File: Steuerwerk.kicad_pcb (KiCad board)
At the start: 2 copper layers, 100 x 160 mm, 332 parts, among them J1 Conn_01x04, J2 Conn_01x02, J3 Conn_01x03, J4 Conn_01x03, J5 Conn_01x02, J6 Conn_01x04, J7 Conn_01x02, J8 Conn_01x04, J9 Conn_01x02, Q1 Q_PNP_BCE, U1 74LS161, U2 74LS138, U3 74LS138, U4 74240, U5 74LS374, U6 74LS374, U7 74541, U8 74541

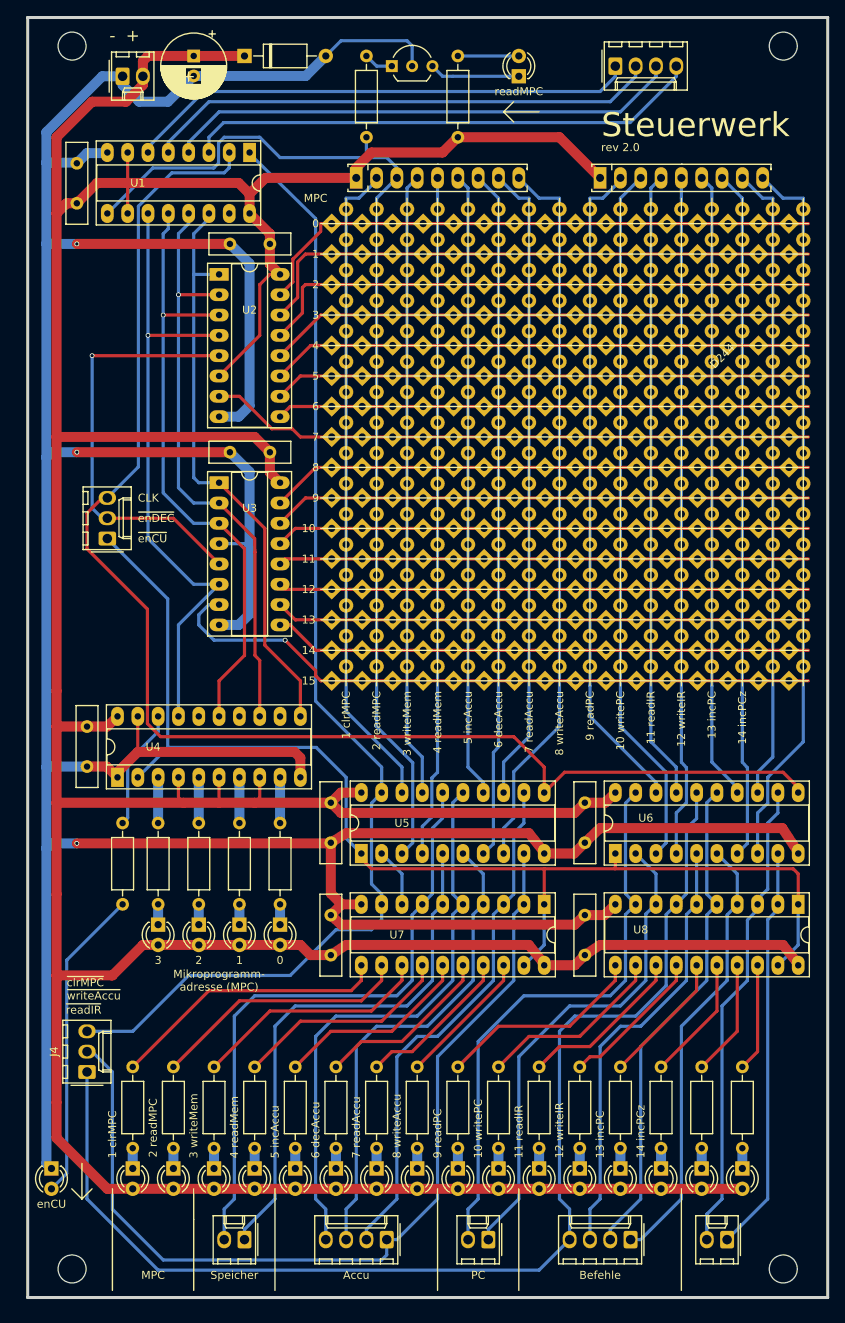
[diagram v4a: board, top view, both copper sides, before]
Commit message: Footprint EuroBoard gedreht und auf das Gitter gelegt (Ursprung links oben)
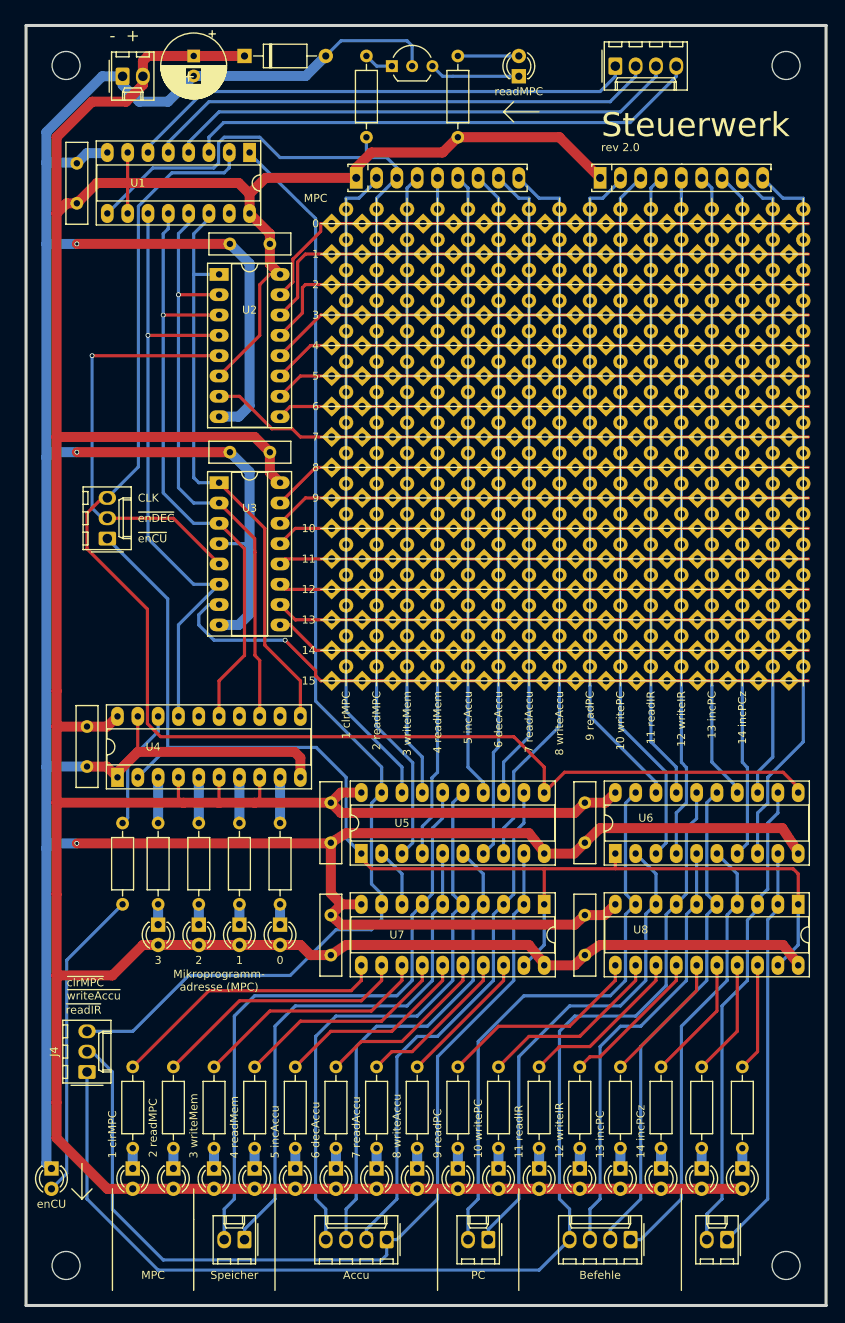
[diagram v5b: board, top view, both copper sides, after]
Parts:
- moved REF** 187.9 mm to (41.3, 33.6), turned to 0 degrees

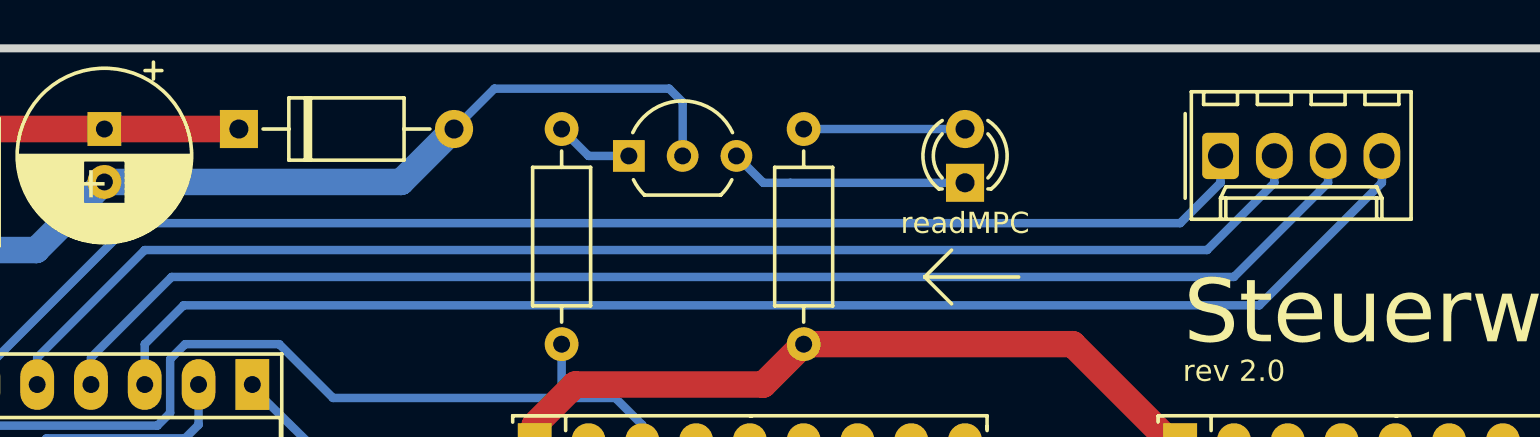
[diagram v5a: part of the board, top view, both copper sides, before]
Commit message: Befehle: An der Platine weitergearbeitet
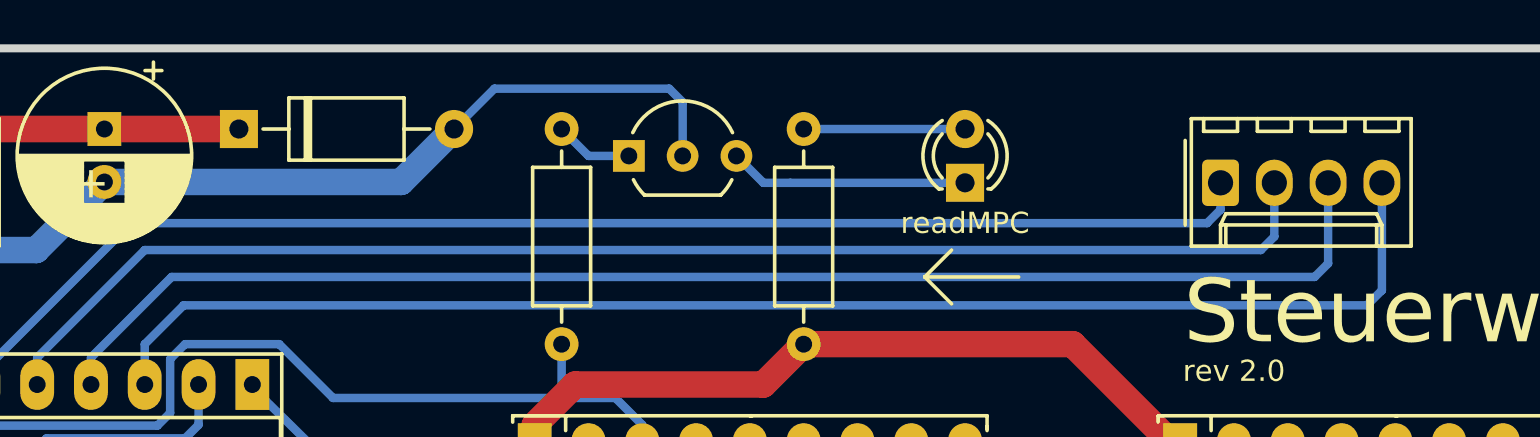
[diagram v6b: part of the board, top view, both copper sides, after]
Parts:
- moved J1 1.27 mm to (115.0, 40.0)
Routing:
- net Net-(J1-Pad4): track 64.8 -> 66.5 mm
- net Net-(J1-Pad3): track 64.4 -> 65.3 mm
- net Net-(J1-Pad1): track 64.0 -> 63.5 mm
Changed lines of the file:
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@@
   )
   (setup
-    (last_trace_width 1.25)
+    (last_trace_width 0.4)
     (user_trace_width 0.2)
     (user_trace_width 0.4)
@@
     (solder_mask_min_width 0.25)
     (aux_axis_origin 0 0)
-    (grid_origin 82.586 52.665998)
+    (grid_origin 41.311 33.615998)
     (visible_elements 7FFFFFFF)
     (pcbplotparams
@@
   )
   (module Connector_Molex:Molex_KK-254_AE-6410-04A_1x04_P2.54mm_Vertical (layer F.Cu)
-    (at 114.971 38.695998)
+    (at 114.971 39.965998)
     (descr "Molex KK-254 Interconnect System, old/engineering part number: AE-6410-04A example for new part number: 22-27-2041, 4 Pins (http://www.molex.com/pdm_docs/sd/022272021_sd.pdf), generated with kicad-footprint-generator")
     (tags "connector Molex KK-254 vertical")
@@
   (segment (start 93.381 39.965998) (end 94.651 39.965998) (width 0.4) (layer B.Cu) (net 21))
   (segment (start 92.111 38.695998) (end 93.381 39.965998) (width 0.4) (layer B.Cu) (net 21))
-  (segment (start 64.171 43.140998) (end 114.336 43.140998) (width 0.4) (layer B.Cu) (net 22))
-  (segment (start 59.091 48.220998) (end 64.171 43.140998) (width 0.4) (layer B.Cu) (net 22))
-  (segment (start 117.511 39.965998) (end 117.511 38.695998) (width 0.4) (layer B.Cu) (net 22))
-  (segment (start 114.336 43.140998) (end 117.511 39.965998) (width 0.4) (layer B.Cu) (net 22))
   (segment (start 59.091 49.490998) (end 59.091 48.220998) (width 0.4) (layer B.Cu) (net 22))
-  (segment (start 113.066 41.870998) (end 114.971 39.965998) (width 0.4) (layer B.Cu) (net 23))
-  (segment (start 63.536 41.870998) (end 113.066 41.870998) (width 0.4) (layer B.Cu) (net 23))
+  (segment (start 59.091 48.220998) (end 64.171 43.140998) (width 0.4) (layer B.Cu) (net 22))
+  (segment (start 64.171 43.140998) (end 116.876 43.140998) (width 0.4) (layer B.Cu) (net 22))
+  (segment (start 117.511 42.505998) (end 117.511 39.965998) (width 0.4) (layer B.Cu) (net 22))
+  (segment (start 116.876 43.140998) (end 117.511 42.505998) (width 0.4) (layer B.Cu) (net 22))
+  (segment (start 114.971 41.235998) (end 114.971 39.965998) (width 0.4) (layer B.Cu) (net 23))
+  (segment (start 114.336 41.870998) (end 114.971 41.235998) (width 0.4) (layer B.Cu) (net 23))
+  (segment (start 63.536 41.870998) (end 114.336 41.870998) (width 0.4) (layer B.Cu) (net 23))
   (segment (start 56.551 48.855998) (end 63.536 41.870998) (width 0.4) (layer B.Cu) (net 23))
-  (segment (start 114.971 39.965998) (end 114.971 38.695998) (width 0.4) (layer B.Cu) (net 23))
   (segment (start 56.551 49.490998) (end 56.551 48.855998) (width 0.4) (layer B.Cu) (net 23))
   (segment (start 126.401 142.200998) (end 127.671 143.470998) (width 0.4) (layer B.Cu) (net 24))
@@
   (segment (start 123.226 180.300998) (end 118.146 185.380998) (width 0.4) (layer B.Cu) (net 25))
   (segment (start 118.146 185.380998) (end 116.876 185.380998) (width 0.4) (layer B.Cu) (net 25))
-  (segment (start 122.591 39.965998) (end 122.591 38.695998) (width 0.4) (layer B.Cu) (net 26))
-  (segment (start 116.806001 45.750997) (end 122.591 39.965998) (width 0.4) (layer B.Cu) (net 26))
-  (segment (start 66.006001 45.750997) (end 116.806001 45.750997) (width 0.4) (layer B.Cu) (net 26))
+  (segment (start 122.591 45.045998) (end 122.591 39.965998) (width 0.4) (layer B.Cu) (net 26))
+  (segment (start 121.886001 45.750997) (end 122.591 45.045998) (width 0.4) (layer B.Cu) (net 26))
+  (segment (start 66.006001 45.750997) (end 121.886001 45.750997) (width 0.4) (layer B.Cu) (net 26))
   (segment (start 64.171 47.585998) (end 66.006001 45.750997) (width 0.4) (layer B.Cu) (net 26))
   (segment (start 64.171 49.490998) (end 64.171 47.585998) (width 0.4) (layer B.Cu) (net 26))
-  (segment (start 120.051 39.965998) (end 120.051 38.695998) (width 0.4) (layer B.Cu) (net 27))
-  (segment (start 115.606 44.410998) (end 120.051 39.965998) (width 0.4) (layer B.Cu) (net 27))
-  (segment (start 65.441 44.410998) (end 115.606 44.410998) (width 0.4) (layer B.Cu) (net 27))
+  (segment (start 120.051 43.775998) (end 120.051 39.965998) (width 0.4) (layer B.Cu) (net 27))
+  (segment (start 119.416 44.410998) (end 120.051 43.775998) (width 0.4) (layer B.Cu) (net 27))
+  (segment (start 65.441 44.410998) (end 119.416 44.410998) (width 0.4) (layer B.Cu) (net 27))
   (segment (start 61.631 48.220998) (end 65.441 44.410998) (width 0.4) (layer B.Cu) (net 27))
   (segment (start 61.631 49.490998) (end 61.631 48.220998) (width 0.4) (layer B.Cu) (net 27))

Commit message: Steuerwerk 2.0 gerber exportiert
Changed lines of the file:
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@@
   )
   (setup
-    (last_trace_width 0.4)
+    (last_trace_width 1.25)
     (user_trace_width 0.2)
     (user_trace_width 0.4)
@@
     (visible_elements 7FFFFFFF)
     (pcbplotparams
-      (layerselection 0x00030_ffffffff)
+      (layerselection 0x010f0_ffffffff)
       (usegerberextensions false)
       (usegerberattributes false)
@@
       (psa4output false)
       (plotreference true)
-      (plotvalue true)
+      (plotvalue false)
       (plotinvisibletext false)
-      (padsonsilk false)
+      (padsonsilk true)
       (subtractmaskfromsilk false)
-      (outputformat 4)
+      (outputformat 1)
       (mirror false)
-      (drillshape 2)
+      (drillshape 0)
       (scaleselection 1)
-      (outputdirectory "C:/Users/Michael/Desktop/gerber-test/"))
+      (outputdirectory "gerber/Steuerwerk 2.0/"))
   )
   (net 0 "")
@@
     (descr "16-lead though-hole mounted DIP package, row spacing 7.62 mm (300 mils), Socket, LongPads")
     (tags "THT DIP DIL PDIP 2.54mm 7.62mm 300mil Socket LongPads")
-    (fp_text reference U3 (at 3.81 3.175) (layer F.SilkS)
+    (fp_text reference U3 (at 3.81 4.445) (layer F.SilkS)
       (effects (font (size 1 1) (thickness 0.17)))
     )
@@
     (descr "20-lead though-hole mounted DIP package, row spacing 7.62 mm (300 mils), Socket, LongPads")
     (tags "THT DIP DIL PDIP 2.54mm 7.62mm 300mil Socket LongPads")
-    (fp_text reference U6 (at 4.445 3.81 180) (layer F.SilkS)
+    (fp_text reference U6 (at 3.81 4.445 180) (layer F.SilkS)
       (effects (font (size 1 1) (thickness 0.17)))
     )
@@
     (descr "20-lead though-hole mounted DIP package, row spacing 7.62 mm (300 mils), Socket, LongPads")
     (tags "THT DIP DIL PDIP 2.54mm 7.62mm 300mil Socket LongPads")
-    (fp_text reference U8 (at 3.175 19.685 180) (layer F.SilkS)
+    (fp_text reference U8 (at 3.81 18.415 180) (layer F.SilkS)
       (effects (font (size 1 1) (thickness 0.17)))
     )
@@
     (effects (font (size 1 1) (thickness 0.17)))
   )
-  (gr_line (start 101.001 44.410998) (end 102.271 45.680998) (layer F.SilkS) (width 0.17))
-  (gr_line (start 102.271 43.140998) (end 101.001 44.410998) (layer F.SilkS) (width 0.17))
-  (gr_line (start 105.446 44.410998) (end 101.001 44.410998) (layer F.SilkS) (width 0.17))
+  (gr_line (start 101.001 44.410998) (end 102.271 45.680998) (layer F.SilkS) (width 0.4))
+  (gr_line (start 102.271 43.140998) (end 101.001 44.410998) (layer F.SilkS) (width 0.4))
+  (gr_line (start 105.446 44.410998) (end 101.001 44.410998) (layer F.SilkS) (width 0.4))
   (gr_text readMPC (at 102.906 41.870998) (layer F.SilkS)
     (effects (font (size 1 1) (thickness 0.17)))
   )
-  (gr_line (start 48.296 180.300998) (end 49.566 179.030998) (layer F.SilkS) (width 0.17))
-  (gr_line (start 48.296 180.300998) (end 47.026 179.030998) (layer F.SilkS) (width 0.17))
-  (gr_line (start 48.296 175.855998) (end 48.296 180.300998) (layer F.SilkS) (width 0.17))
+  (gr_line (start 48.296 180.300998) (end 49.566 179.030998) (layer F.SilkS) (width 0.4))
+  (gr_line (start 48.296 180.300998) (end 47.026 179.030998) (layer F.SilkS) (width 0.4))
+  (gr_line (start 48.296 175.855998) (end 48.296 180.300998) (layer F.SilkS) (width 0.4))
   (gr_text 3 (at 57.821 150.455998) (layer F.SilkS)
     (effects (font (size 1 1) (thickness 0.17)))
@@
   (gr_line (start 85.126 115.530998) (end 85.126 55.205998) (layer F.SilkS) (width 0.17))
   (gr_line (start 81.316 55.205998) (end 81.316 115.530998) (layer F.SilkS) (width 0.17))
-  (gr_text + (at 54.646 34.885998) (layer F.SilkS)
+  (gr_text + (at 55.916 34.885998) (layer F.SilkS)
     (effects (font (size 1.5 1.5) (thickness 0.17)))
   )
-  (gr_text - (at 52.106 34.885998) (layer F.SilkS)
+  (gr_text - (at 53.376 34.885998) (layer F.SilkS)
     (effects (font (size 1.5 1.5) (thickness 0.17)))
   )

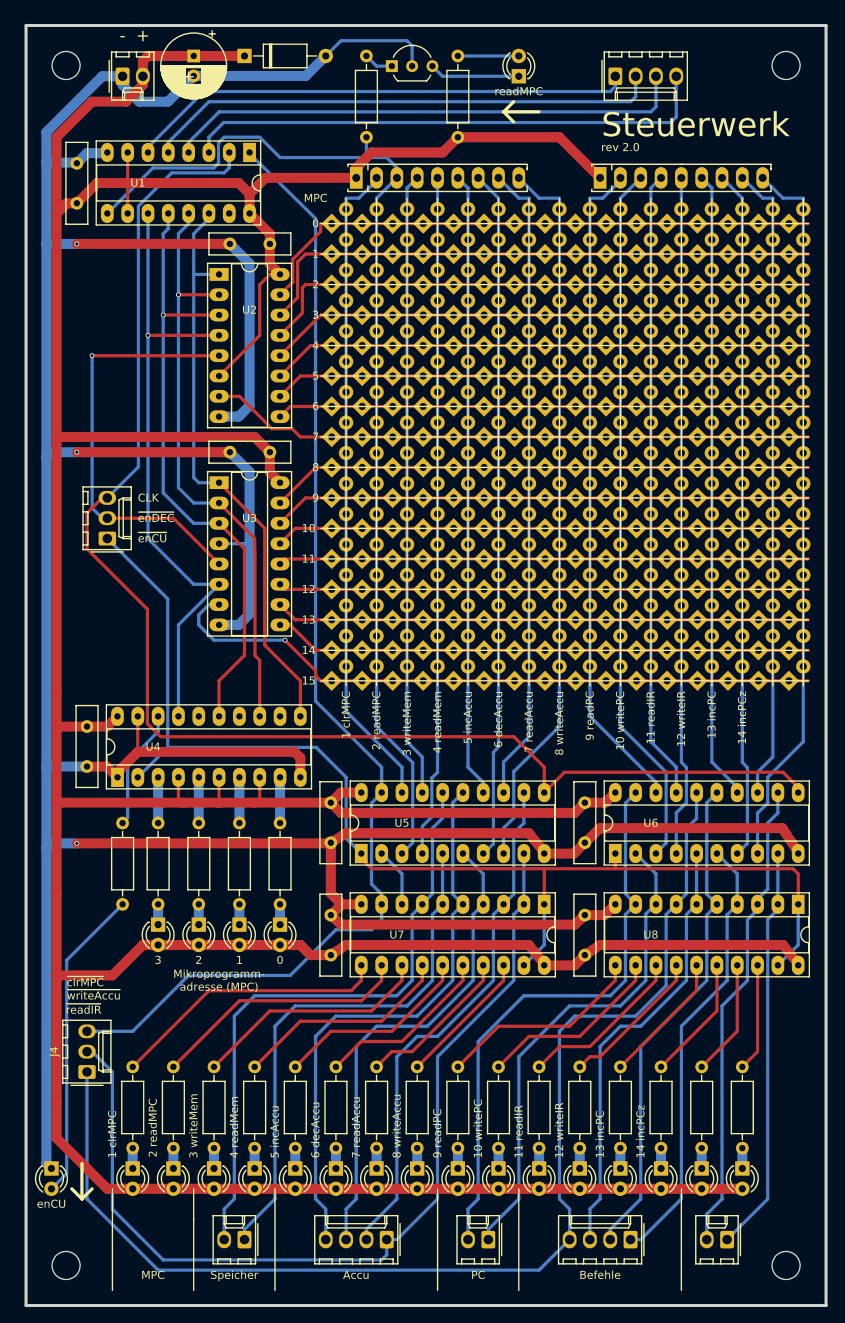
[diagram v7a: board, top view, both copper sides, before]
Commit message: Befehle und Steuerwerk: - Kleinkram - gerber rev 2.0 für Bestellung exportiert
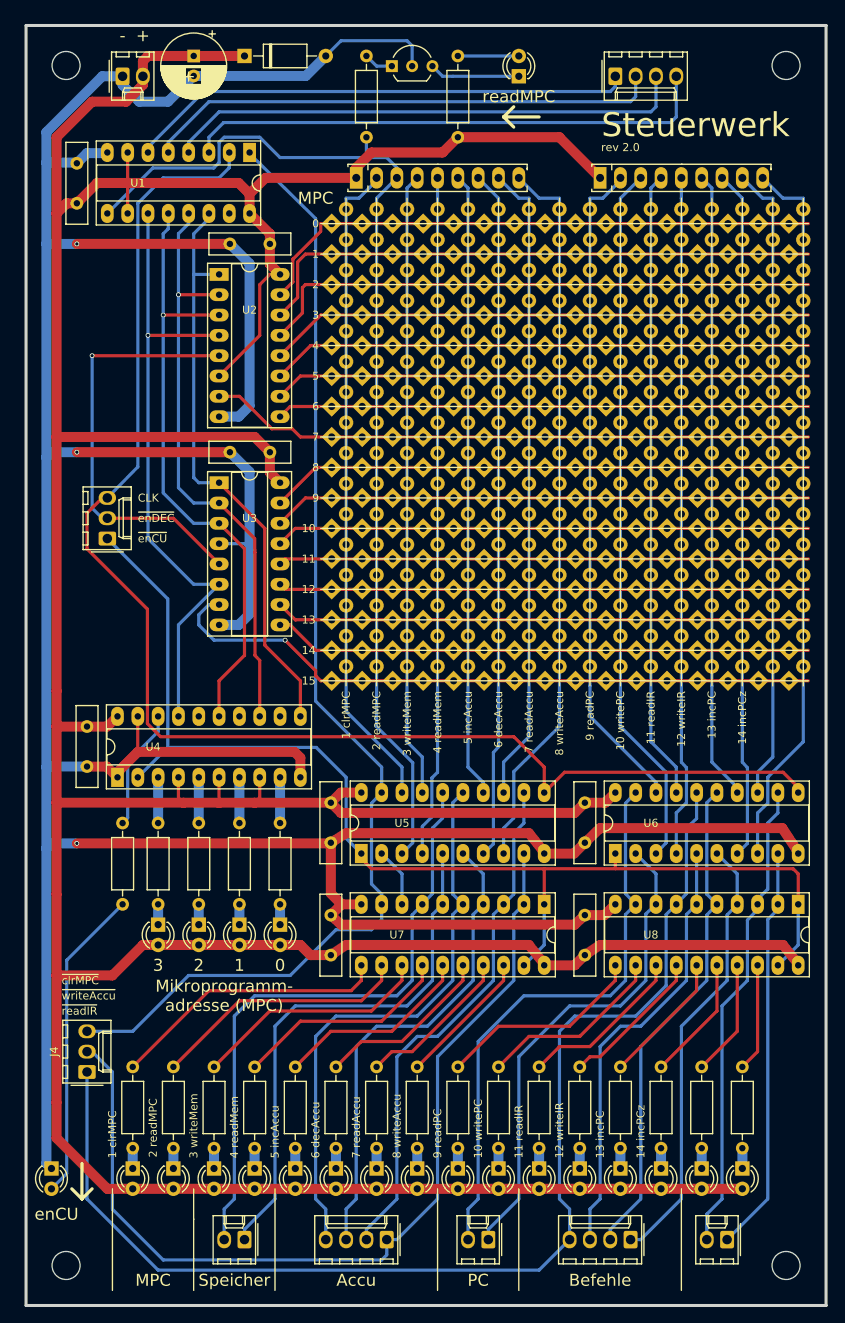
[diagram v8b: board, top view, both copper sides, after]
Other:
- rule pad_to_mask_clearance: 0 -> 0.08
- rule solder_mask_min_width: 0.25 -> 0.254
